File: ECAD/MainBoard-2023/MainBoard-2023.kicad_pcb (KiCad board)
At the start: 2 copper layers, 60 x 150 mm, 89 parts, among them J1 XT60, J10 Conn_01x14, J11 Conn_01x03, J12 Conn_01x04, J13 Conn_01x03, J14 Conn_01x03, J15 Conn_01x03, J16 XT30, J17 XT30, J2 Conn_01x04, J20 BAU, J21 BAU, J22 Conn_01x04, J23 Conn_01x02, J24 Conn_01x07, J26 BAU, J27 BAU, J28 Conn_01x02, J29 Conn_01x02, J3 ConStep1, J30 Conn_01x03, J32 Conn_01x02, J37 Conn_01x02, J38 Conn_01x02, J39 Conn_01x02, J4 Conn_01x02, J40 Conn_01x02, J5 ConStep1, J6 ConStep1, J7 XT30, J8 Conn_01x02, J9 XT60, K1 CB1-P-24V, U1 Teensy3.5_All_Pins, U2 R-78B3.3-2.0, U4 R-78B5.0-2.0

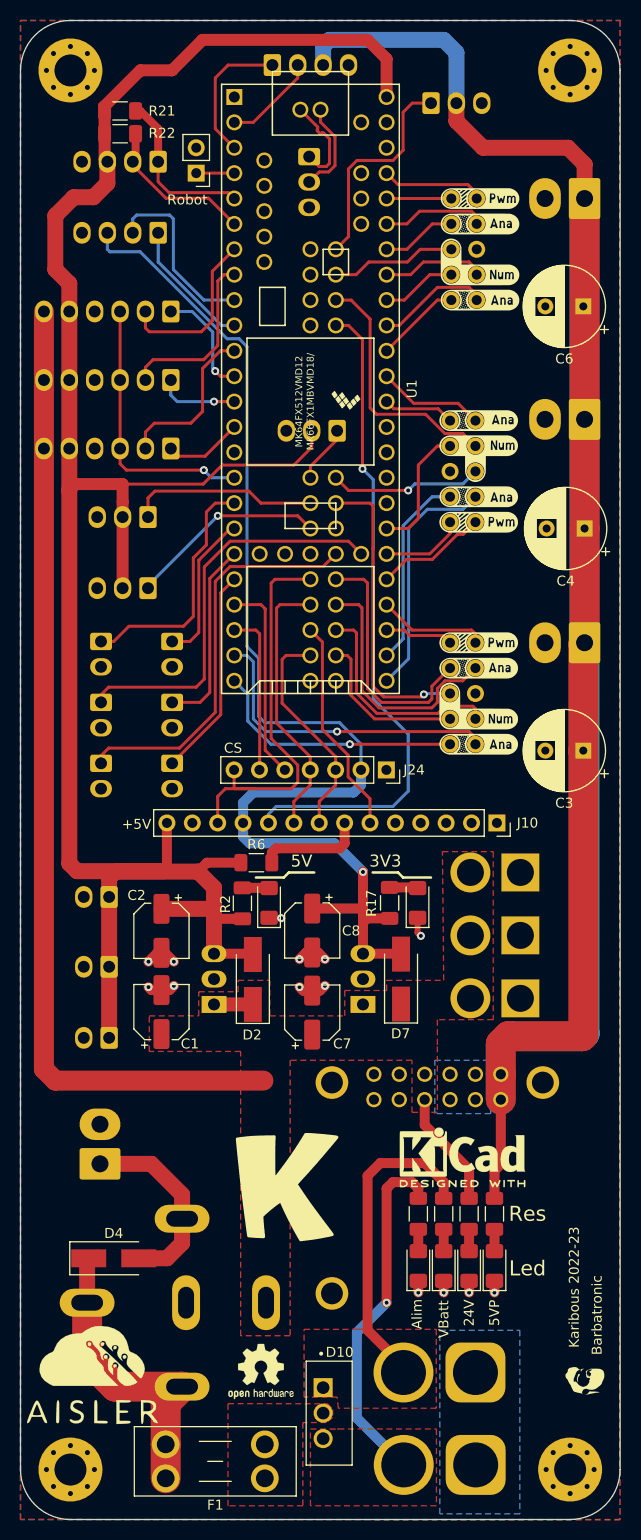
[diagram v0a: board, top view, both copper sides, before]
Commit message: Silkscreen and 3d models MainBoard 2023
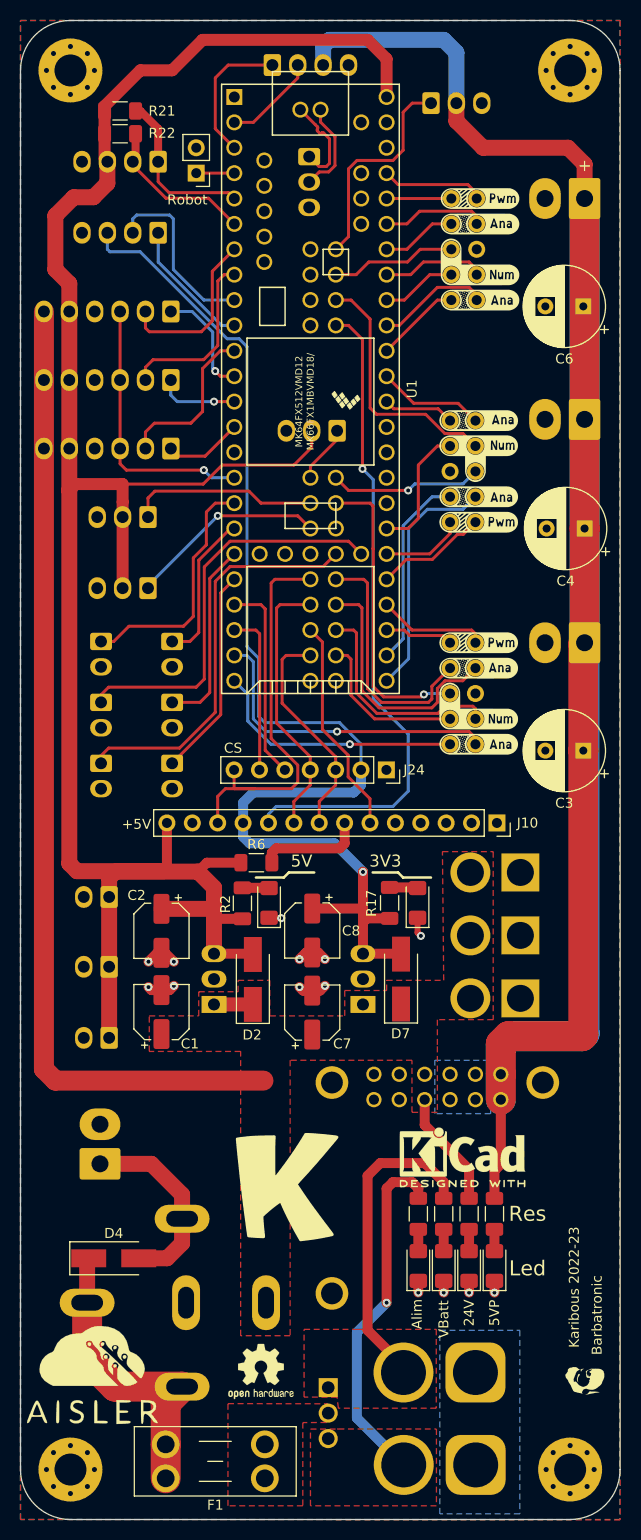
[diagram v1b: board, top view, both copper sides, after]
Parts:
- added G***: LOGO, LOGO, B.Cu at (108.2, 108.3)
- D10: moved to B.Cu
- moved D10 0.51 mm to (121.8, 162.8)
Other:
- board text added: "DC"
- board text added: "Miso"
- board text added: "Mosi"
- board text added: "SCK"
